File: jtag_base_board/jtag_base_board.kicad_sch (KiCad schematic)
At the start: 0 parts

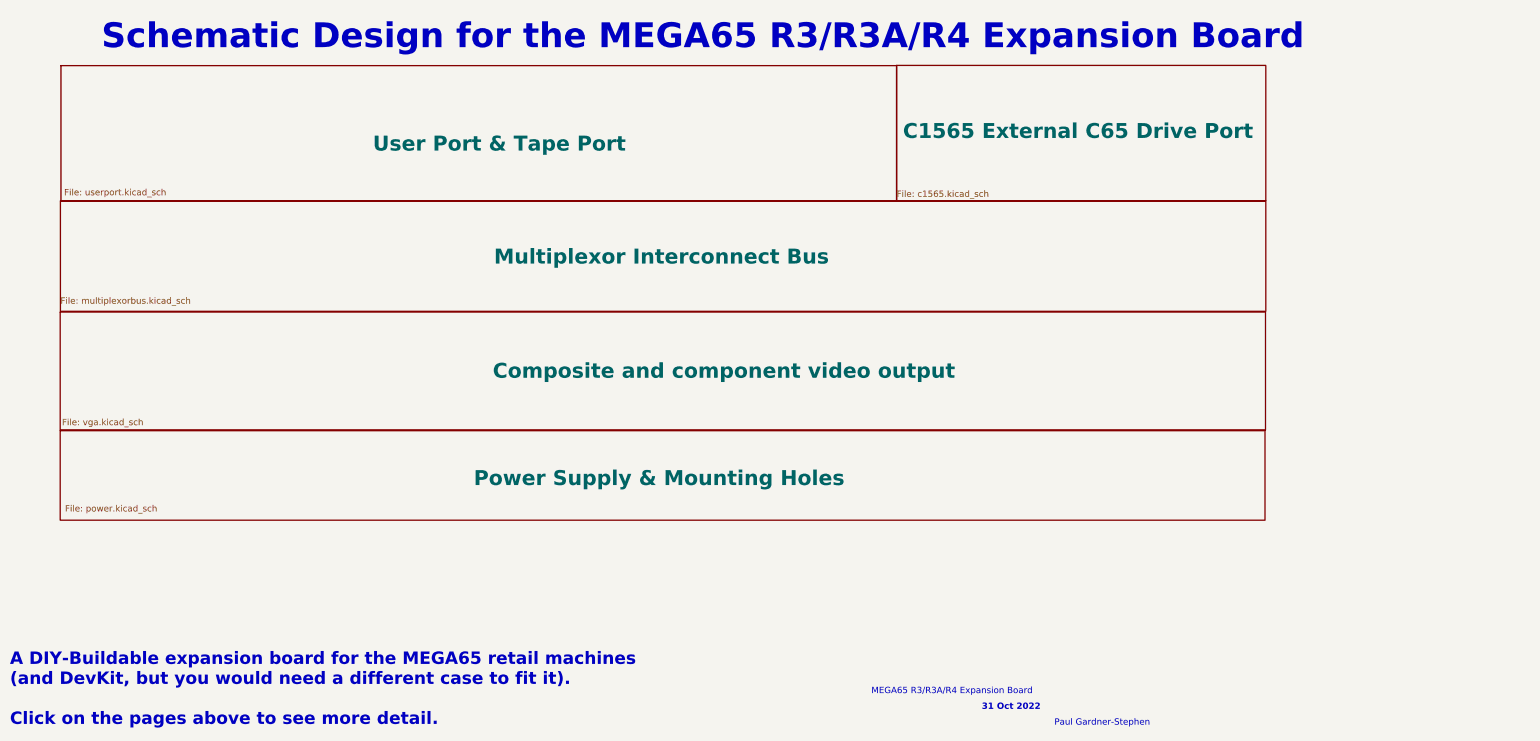
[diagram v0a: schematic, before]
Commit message: Delete the schematics that aren't used by the jtag base board
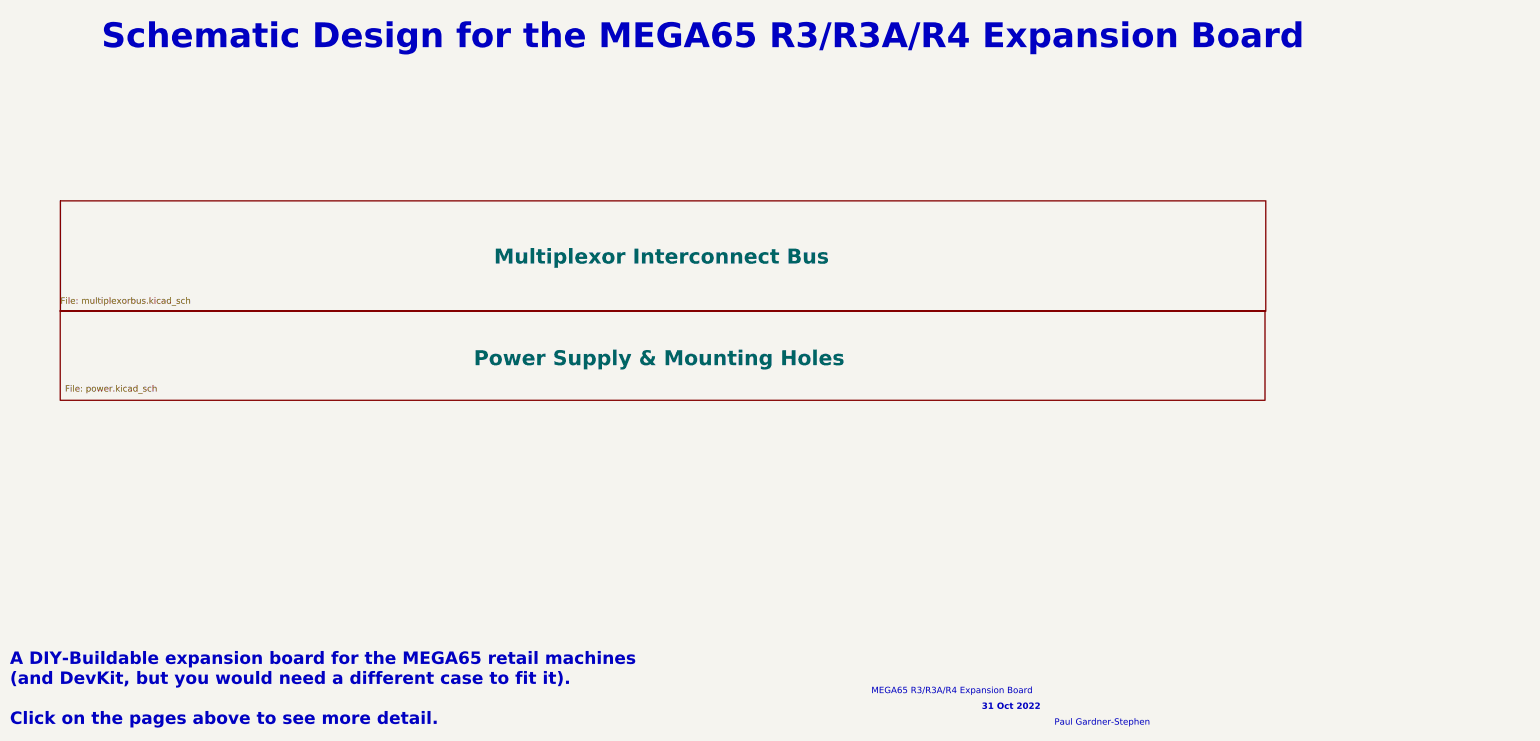
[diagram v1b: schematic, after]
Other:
- removed sheet C1565 External C65 Drive Port
- removed sheet Composite and component video output
- removed sheet User Port & Tape Port
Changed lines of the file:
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@@
-	)
-	(sheet
-		(at 26.1366 63.8175)
-		(size 168.1734 27.2415)
-		(exclude_from_sim no)
-		(in_bom yes)
-		(on_board yes)
-		(dnp no)
-		(stroke
-			(width 0.25)
-			(type solid)
-		)
-		(fill
-			(color 54 142 255 1)
-		)
-		(property "Sheetname" "User Port & Tape Port"
-			(at 88.9 81.28 0)
-			(show_name no)
-			(do_not_autoplace no)
-			(effects
-				(font
-					(size 3 3)
-					(bold yes)
-				)
-				(justify left bottom)
-			)
-		)
-		(property "Sheetfile" "userport.kicad_sch"
-			(at 26.7716 88.5825 0)
-			(show_name no)
-			(do_not_autoplace no)
-			(effects
-				(font
-					(size 1.27 1.27)
-				)
-				(justify left top)
-			)
-		)
-		(instances
-			(project "jtag_base_board"
-				(path "/e63e39d7-6ac0-4ffd-8aa3-1841a4541b55"
-					(page "7")
-				)
-			)
-		)
-	)
-	(sheet
-		(at 194.3072 63.7735)
-		(size 74.2938 27.2606)
-		(exclude_from_sim no)
-		(in_bom yes)
-		(on_board yes)
-		(dnp no)
-		(stroke
-			(width 0.25)
-			(type solid)
-		)
-		(fill
-			(color 0 0 255 1)
-		)
-		(property "Sheetname" "C1565 External C65 Drive Port"
-			(at 195.58 78.74 0)
-			(show_name no)
-			(do_not_autoplace no)
-			(effects
-				(font
-					(size 3 3)
-					(bold yes)
-				)
-				(justify left bottom)
-			)
-		)
-		(property "Sheetfile" "c1565.kicad_sch"
-			(at 194.31 88.9 0)
-			(show_name no)
-			(do_not_autoplace no)
-			(effects
-				(font
-					(size 1.27 1.27)
-				)
-				(justify left top)
-			)
-		)
-		(instances
-			(project "jtag_base_board"
-				(path "/e63e39d7-6ac0-4ffd-8aa3-1841a4541b55"
-					(page "6")
-				)
-			)
-		)
-	)
-	(sheet
-		(at 25.9969 113.411)
-		(size 242.5573 23.6982)
-		(exclude_from_sim no)
-		(in_bom yes)
-		(on_board yes)
-		(dnp no)
-		(stroke
-			(width 0.25)
-			(type solid)
-		)
-		(fill
-			(color 255 208 70 1)
-		)
-		(property "Sheetname" "Composite and component video output"
-			(at 113.03 127 0)
-			(show_name no)
-			(do_not_autoplace no)
-			(effects
-				(font
-					(size 3 3)
-					(bold yes)
-				)
-				(justify left bottom)
-			)
-		)
-		(property "Sheetfile" "vga.kicad_sch"
-			(at 26.3398 134.8486 0)
-			(show_name no)
-			(do_not_autoplace no)
-			(effects
-				(font
-					(size 1.27 1.27)
-				)
-				(justify left top)
-			)
-		)
-		(instances
-			(project "jtag_base_board"
-				(path "/e63e39d7-6ac0-4ffd-8aa3-1841a4541b55"
-					(page "10")
-				)
-			)
-		)
 	)
 	(sheet
@@
 	)
 	(sheet
-		(at 25.9969 137.287)
+		(at 25.9969 113.157)
 		(size 242.4557 18.0086)
 		(exclude_from_sim no)
@@
 		)
 		(property "Sheetname" "Power Supply & Mounting Holes"
-			(at 109.22 148.59 0)
+			(at 109.22 124.46 0)
 			(show_name no)
 			(do_not_autoplace no)
@@
 		)
 		(property "Sheetfile" "power.kicad_sch"
-			(at 26.9494 152.2095 0)
+			(at 26.9494 128.0795 0)
 			(show_name no)
 			(do_not_autoplace no)
